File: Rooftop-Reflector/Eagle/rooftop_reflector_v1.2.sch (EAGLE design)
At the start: 18 parts, among them Q1 MOSFET-NCH, Q4 MOSFET-NCH, U1 ADAFRUIT_LEONARDO, X1 MSTBA4

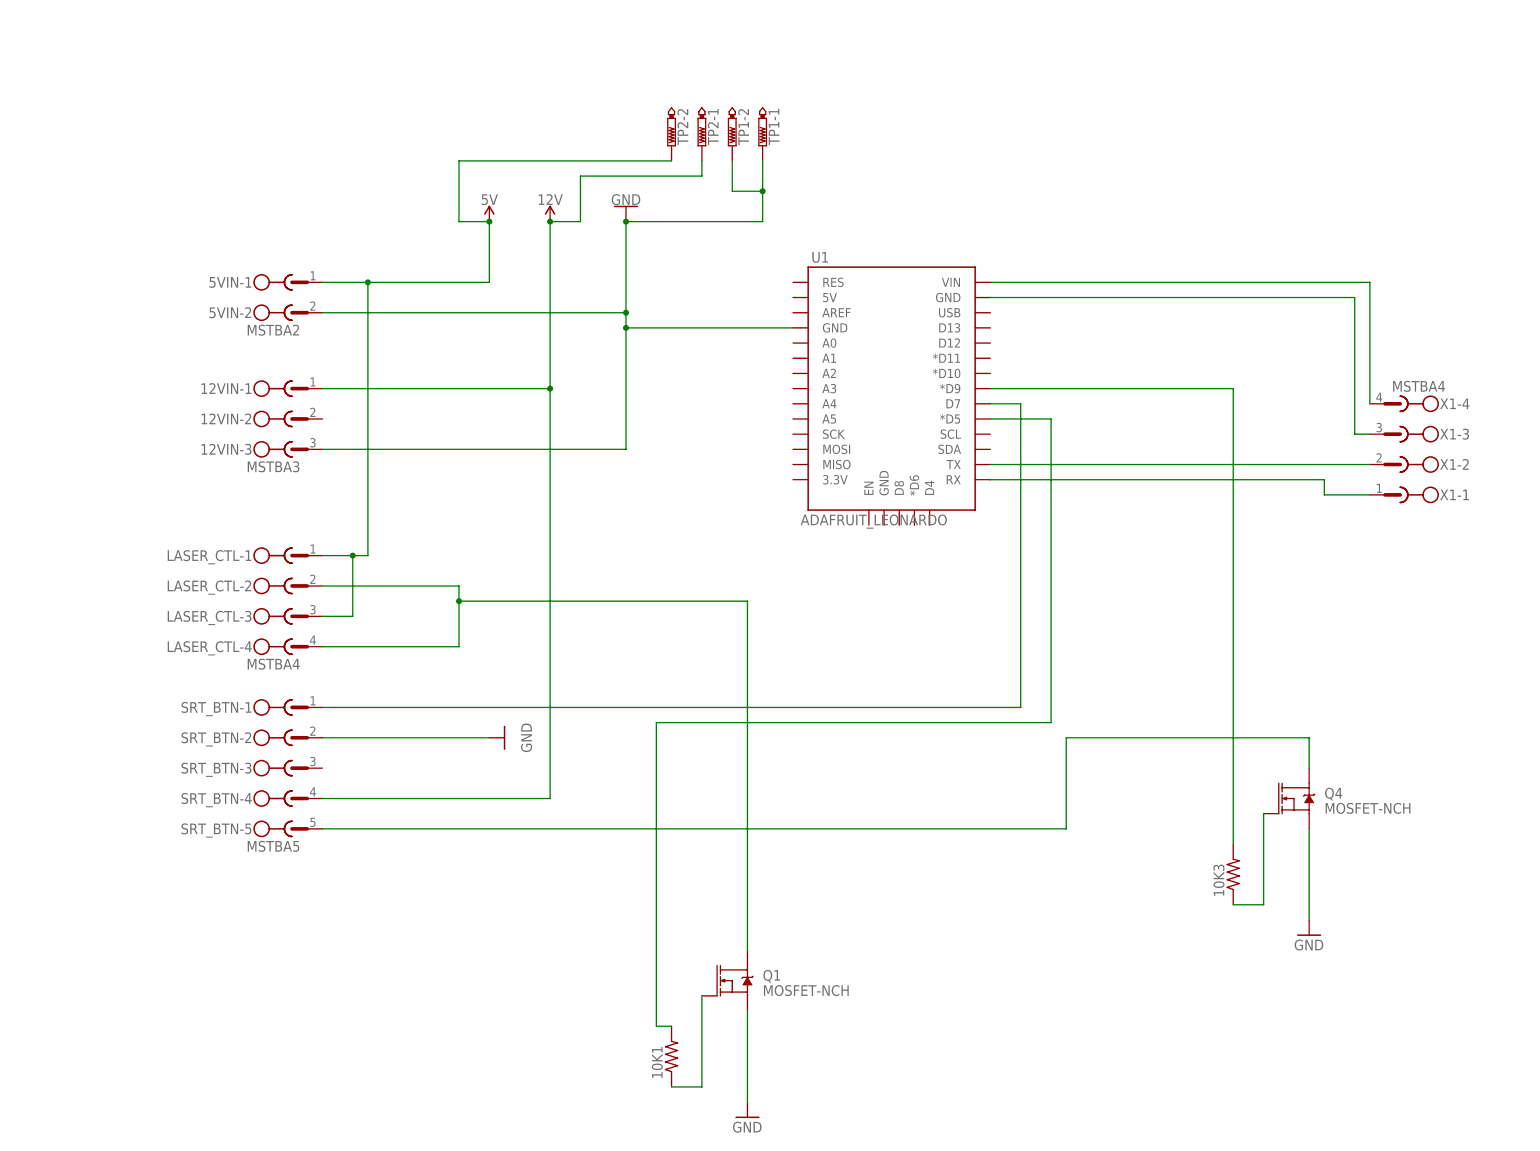
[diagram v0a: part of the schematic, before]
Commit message: Updated Btn calls and added Pulse function
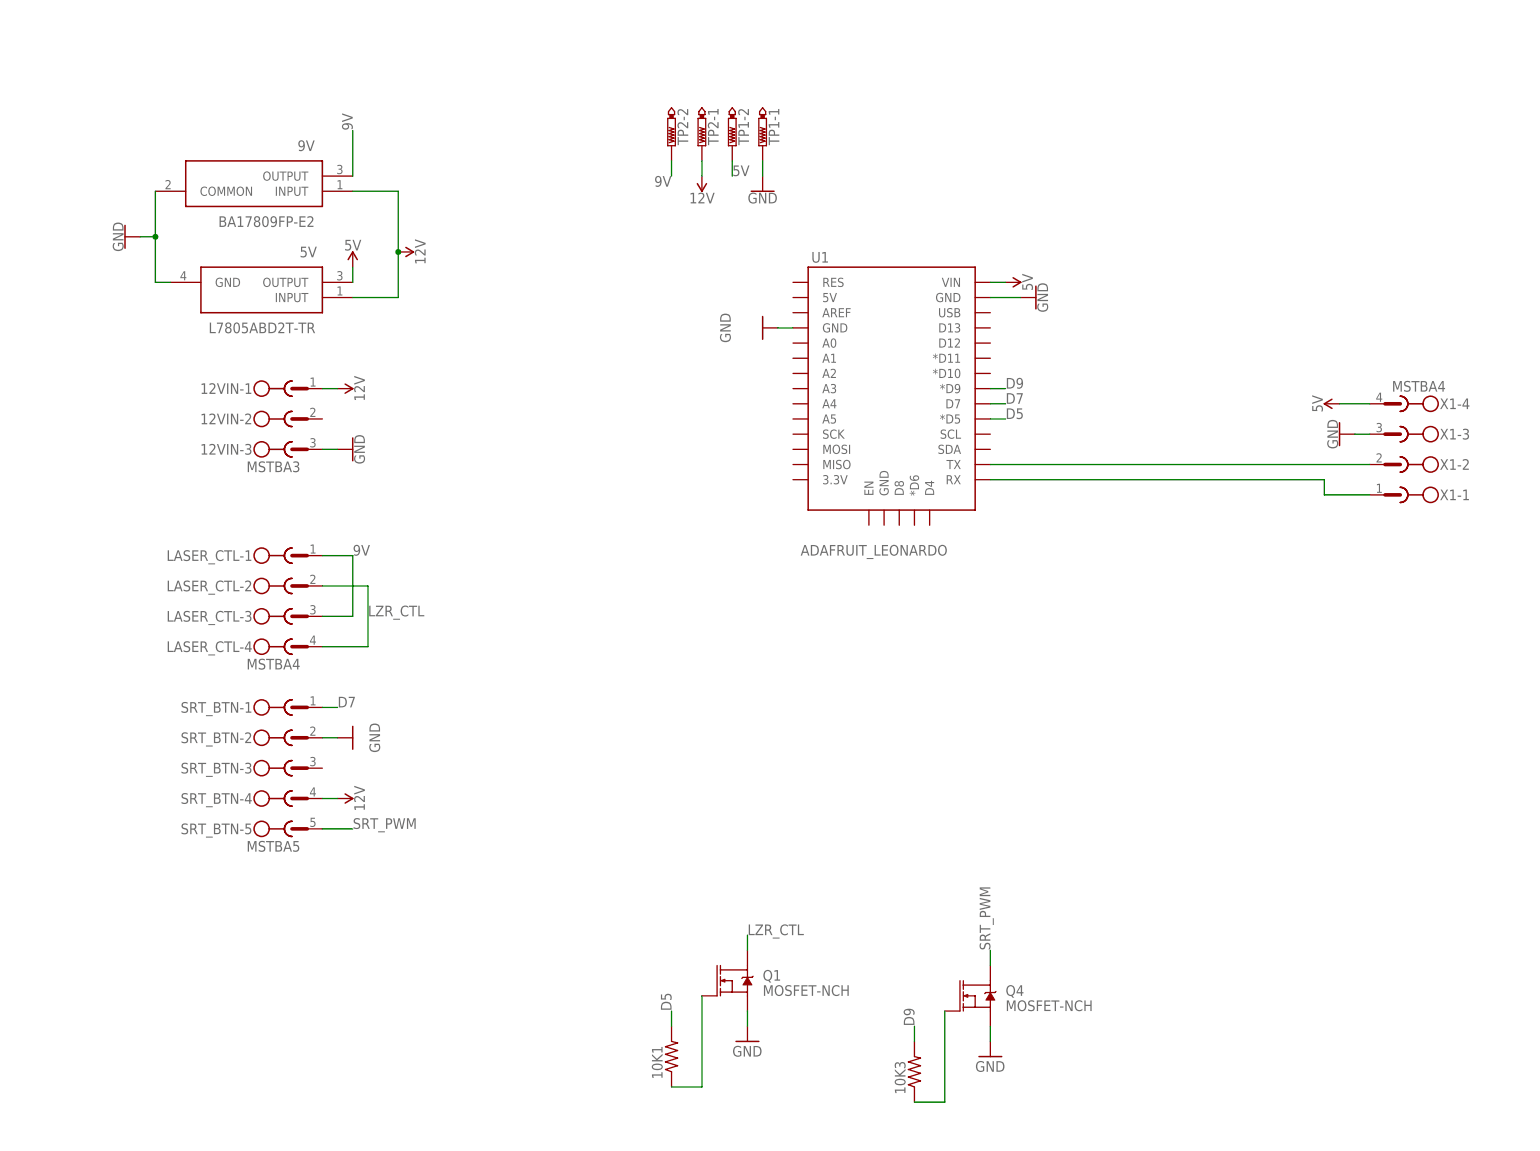
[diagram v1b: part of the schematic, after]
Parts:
- removed 5VIN: MSTBA2, con-phoenix-508:MSTBA2
- added 5V: L7805ABD2T-TR, SamacSys_Parts:L7805ABD2T-TR
- added 9V: BA17809FP-E2, SamacSys_Parts:BA17809FP-E2
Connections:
- net N$1 renamed D9
- net N$2 renamed D7
- net N$3 renamed SRT_PWM
- net N$5 renamed D5
- net N$6 renamed LZR_CTL
- removed net N$10: U1.GND@2, X1-3.1
- removed net N$9: U1.VIN, X1-4.1
- new net 9V: 9V.OUTPUT, LASER_CTL-1.1, LASER_CTL-3.1, TP2-2.TP
- net 12V: now also 5V.INPUT, 9V.INPUT
- net 5V: now also 5V.OUTPUT, TP1-2.TP, U1.VIN, X1-4.1; no longer 5VIN-1.1, LASER_CTL-1.1, LASER_CTL-3.1, TP2-2.TP
- net GND: now also 5V.GND, 9V.COMMON, U1.GND@2, X1-3.1; no longer 5VIN-2.1, TP1-2.TP
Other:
- moved on the sheet: 10K3, Q4
